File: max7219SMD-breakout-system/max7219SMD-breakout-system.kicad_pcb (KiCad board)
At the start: 2 copper layers, 80 x 80 mm, 34 parts, among them IC1 MAX7219CNG, IC2 MAX7219CNG, IC3 MAX7219CNG, IC4 MAX7219CNG, J1 Conn_01x02_Male, J10 Conn_02x08_Odd_Even, J11 Conn_01x05_Male, J2 Conn_01x05_Male, J3 Conn_02x08_Odd_Even, J4 Conn_02x08_Odd_Even, J5 Conn_02x08_Odd_Even, J6 Conn_02x08_Odd_Even, J7 Conn_02x08_Odd_Even, J8 Conn_02x08_Odd_Even, J9 Conn_02x08_Odd_Even

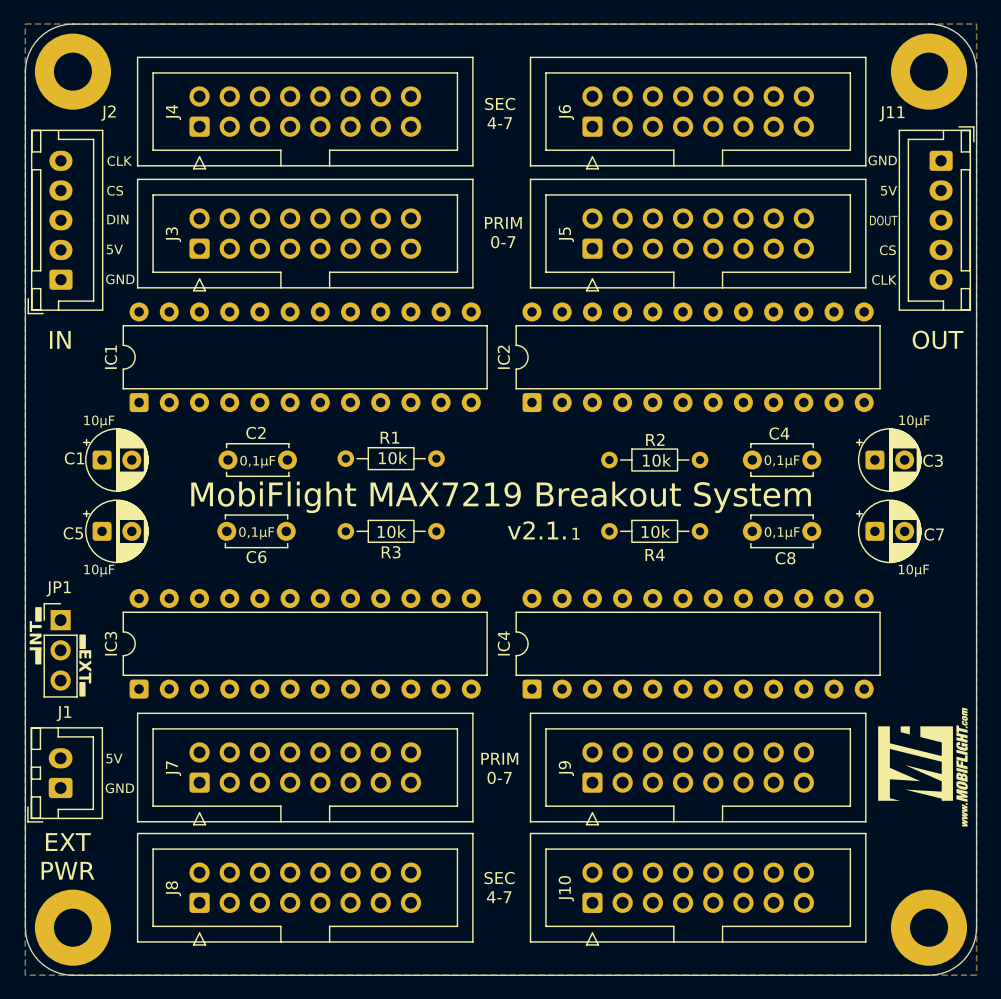
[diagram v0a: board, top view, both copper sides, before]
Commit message: everything routed
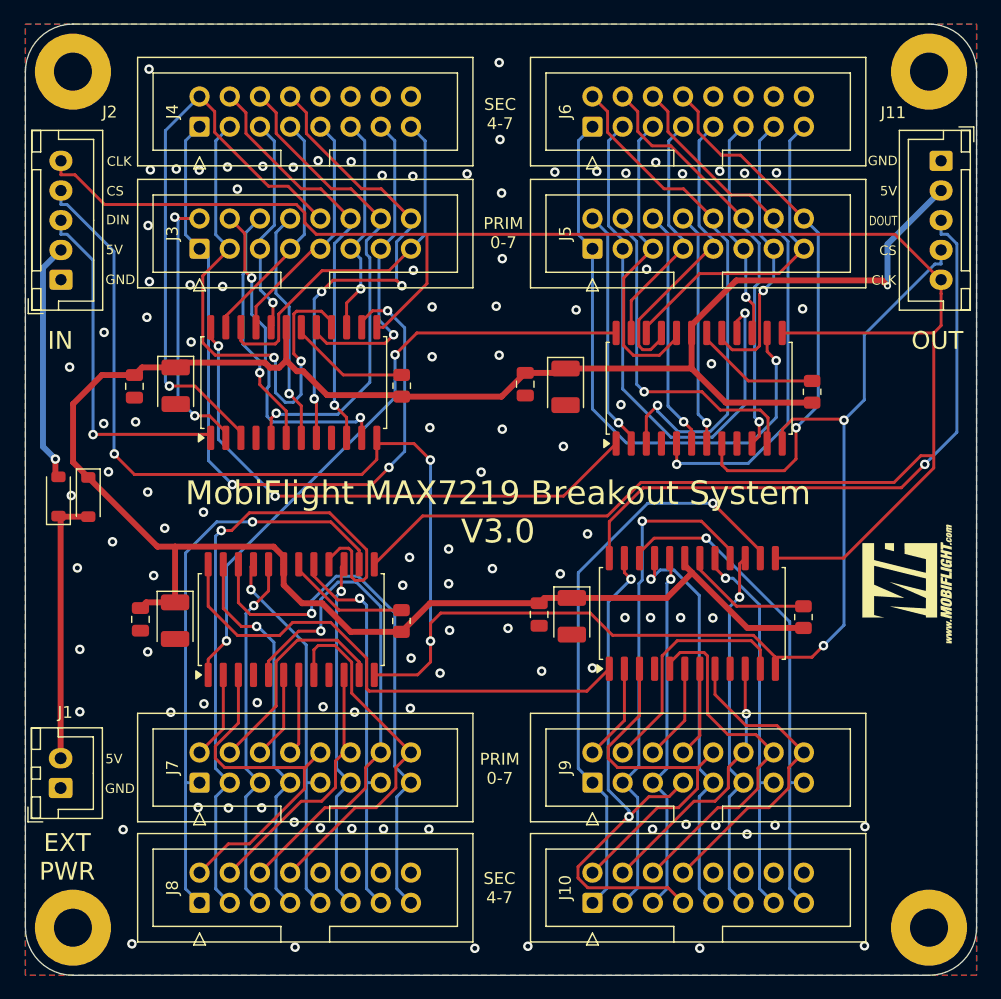
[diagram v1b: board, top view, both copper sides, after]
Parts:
- removed JP1: Jumper_3_Open, Connector_PinHeader_2.54mm:PinHeader_1x03_P2.54mm_Vertical
- added D1: D_Schottky_B5819W-SL, Diode_SMD:D_SOD-123, F.Cu at (55.5, 56.5)
- added D2: D_Schottky_B5819W-SL, Diode_SMD:D_SOD-123, F.Cu at (58.0, 56.6)
- C1, C3, C5, C7: value 10µF -> 47uF; footprint Capacitor_THT:CP_Radial_D5.0mm_P2.50mm -> Capacitor_Tantalum_SMD:CP_EIA-3528-21_Kemet-B
- C2, C4, C6, C8: value 0,1µF -> 100nF; footprint Capacitor_THT:C_Disc_D5.0mm_W2.5mm_P5.00mm -> Capacitor_SMD:C_0805_2012Metric
- IC1, IC2, IC3, IC4: footprint Package_DIP:DIP-24_W7.62mm -> Package_SO:SOIC-24W_7.5x15.4mm_P1.27mm
- R1, R2, R3, R4: footprint Resistor_THT:R_Axial_DIN0204_L3.6mm_D1.6mm_P7.62mm_Horizontal -> Resistor_SMD:R_0805_2012Metric
- moved C3 26.7 mm to (98.1, 47.3), turned to -90 degrees
- moved C7 26.5 mm to (98.6, 66.6), turned to -90 degrees
- moved C4 20.1 mm to (94.7, 47.1), turned to -90 degrees
- moved C8 19.2 mm to (95.9, 66.5), turned to -90 degrees
- moved R2 18.0 mm to (118.9, 47.7), turned to 90 degrees
- moved R4 17.8 mm to (118.1, 66.7), turned to 90 degrees
- moved G2 15.5 mm to (126.8, 63.9)
- moved IC4 14.9 mm to (108.8, 66.4)
- moved C6 14.3 mm to (62.4, 66.9), turned to -90 degrees
- moved C2 14.3 mm to (61.9, 47.3), turned to -90 degrees
- moved IC2 14.1 mm to (109.4, 47.4)
- moved IC3 14.1 mm to (75.0, 66.9)
- moved IC1 13.1 mm to (75.3, 47.0)
- moved C5 9.70 mm to (65.3, 67.0), turned to -90 degrees
- moved R3 8.87 mm to (84.3, 67.0), turned to 90 degrees
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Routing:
- net VCC: track 0.00 -> 188.9 mm, vias 0 -> 1
- net CLK: track 0.00 -> 185.4 mm
- net CS: track 0.00 -> 160.7 mm, vias 0 -> 5
- net SEG_A1: track 0.00 -> 63.3 mm, vias 0 -> 3
- net SEG_B3: track 0.00 -> 55.9 mm, vias 0 -> 1
- net DOUT4: track 0.00 -> 54.1 mm, vias 0 -> 1
- net DOUT2: track 0.00 -> 52.8 mm, vias 0 -> 2
- net SEG_A2: track 0.00 -> 49.7 mm, vias 0 -> 1
- net SEG_A4: track 0.00 -> 49.3 mm, vias 0 -> 1
- net DIG4_1: track 0.00 -> 49.2 mm, vias 0 -> 1
- net SEG_A3: track 0.00 -> 49.0 mm, vias 0 -> 1
- net DOUT1: track 0.00 -> 47.0 mm, vias 0 -> 2
- net SEG_DP3: track 0.00 -> 46.0 mm, vias 0 -> 1
- net SEG_D4: track 0.00 -> 45.9 mm, vias 0 -> 2
- net SEG_B2: track 0.00 -> 45.8 mm, vias 0 -> 1
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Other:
- board text added: "MobiFlight MAX7219 Breakout System V${REVISION}"
- board text removed: "0,1µF"
- board text removed: "1"
- board text removed: "10k"
- board text removed: "10µF"
- board text removed: "EXT"
- board text removed: "INT"
- board text removed: "MobiFlight MAX7219 Breakout System"
- board text removed: "Power source selection"
- board text removed: "v2.1."

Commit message: PCB optimazations
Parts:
- moved C3 1.31 mm to (99.2, 48.0)
- moved C4 1.31 mm to (95.8, 47.8)
- moved G1 0.78 mm to (93.1, 60.7)
- moved IC4 0.58 mm to (109.4, 66.4)
- moved R4 0.46 mm to (118.6, 66.7)
- moved C7 0.42 mm to (99.1, 66.6)
- moved C8 0.42 mm to (96.3, 66.5)
- moved R2 0.27 mm to (118.6, 47.7)
- moved IC3 0.21 mm to (75.3, 66.9)
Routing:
- net SEG_B3: track 55.9 -> 44.6 mm
- net SEG_B1: track 43.5 -> 36.3 mm, vias 2 -> 0
- net DOUT1: track 47.0 -> 52.3 mm
- net SEG_D4: track 45.9 -> 41.7 mm
- net CLK: track 185.4 -> 189.4 mm, vias 0 -> 4
- net DIG0_1: track 23.2 -> 19.4 mm, vias 2 -> 1
- net SEG_DP3: track 46.0 -> 49.8 mm
- net SEG_A1: track 63.3 -> 66.8 mm
- net VCC: track 188.9 -> 192.2 mm, vias 1 -> 0
- net SEG_G2: track 24.1 -> 22.0 mm
- net DIG6_1: track 41.1 -> 43.0 mm
- net SEG_A4: track 49.3 -> 51.1 mm
- net DIG6_3: track 43.4 -> 45.2 mm
- net DOUT3: track 43.4 -> 45.1 mm
- net DIG1_4: track 20.2 -> 21.7 mm
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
